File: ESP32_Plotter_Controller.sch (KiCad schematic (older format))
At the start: 45 parts, among them J1 ARM JTAG 10pin, J10 Pen Lift, J11 Vselect, J12 X Motor, J13 Y Motor, J14 Neo Pixel LEDs, J15 Pen Direction, J16 Aux Port (I2C), J17 USB_B_Micro, J18 E-Stop, J19 Y Limit Switch, J2 Power, J3 5V Aux, J4 Vin Aux, J5 X Limit Switch, J6 Aux Port (SPI), J7 X Limit, J8 Micro_SD_Card_TF-01A, J9 Y Limit, SW1 RESET, SW2 BOOT, U1 ESP32-WROOM-32D, U2 TMC2130, U3 TMC2130, U4 XL1509, U5 CH340C, U6 AMS1117-3.3

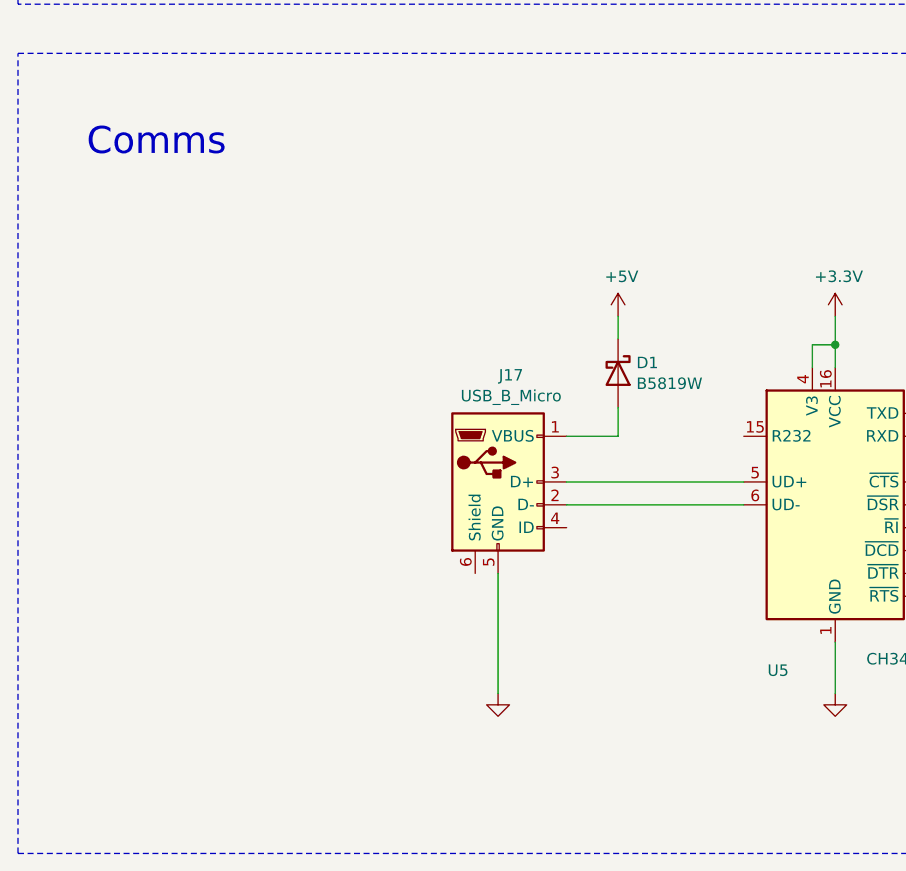
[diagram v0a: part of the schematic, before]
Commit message: Change to USB C connector
Had to move connectors around to make room.
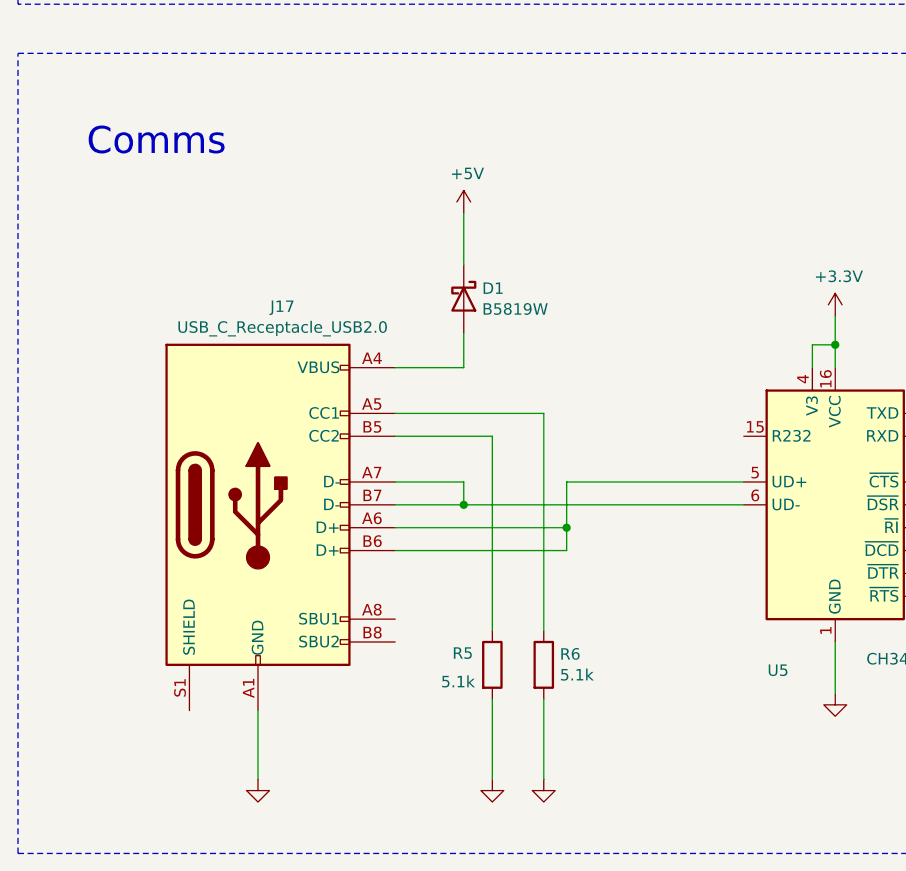
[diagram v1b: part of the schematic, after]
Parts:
- removed J17: USB_B_Micro, Connector_USB:USB_Micro-B_Molex-105017-0001, symbol Connector:USB_B_Micro
- added J17: USB_C_Receptacle_USB2.0, Connector_USB:USB_C_Receptacle_HRO_TYPE-C-31-M-12, symbol Connector:USB_C_Receptacle_USB2.0
- added R5, R6: 5.1k, Resistor_SMD:R_0603_1608Metric, symbol Device:R
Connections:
- net GND: now also J17.A1 (GND), J17.A12 (GND), J17.B1 (GND), J17.B12 (GND), R5.2, R6.2
- net at D1.2 (A): now also J17.A4 (VBUS), J17.A9 (VBUS), J17.B4 (VBUS), J17.B9 (VBUS)
- net at U5.5 (UD+): now also J17.A6 (D+), J17.B6 (D+)
- net at U5.6 (UD-): now also J17.A7 (D-), J17.B7 (D-)
- new net: J17.A5 (CC1), R6.1
- new net: J17.B5 (CC2), R5.1
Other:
- moved on the sheet: D1
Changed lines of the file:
@@
 	4325 12250 4325 12475
-$Comp
-L Connector:USB_B_Micro J17
-U 1 1 618FF665
-P 2850 11550
-F 0 "J17" H 2907 12017 50  0000 C CNN
-F 1 "USB_B_Micro" H 2907 11926 50  0000 C CNN
-F 2 "Connector_USB:USB_Micro-B_Molex-105017-0001" H 3000 11500 50  0001 C CNN
-F 3 "~" H 3000 11500 50  0001 C CNN
-F 4 "C381143" H 2850 11550 50  0001 C CNN "LCSC"
-	1    2850 11550
-	1    0    0    -1
-$EndComp
 $Comp
 L power:GND #NetPort07
 U 1 1 61900AC5
-P 2850 12475
-F 0 "#NetPort07" H 2850 12475 50  0001 C CNN
-F 1 "GND" H 2850 12475 50  0001 C CNN
-F 2 "" H 2850 12475 50  0001 C CNN
-F 3 "" H 2850 12475 50  0001 C CNN
-	1    2850 12475
-	1    0    0    -1
-$EndComp
-Wire Wire Line
-	2850 12475 2850 11950
-Wire Wire Line
-	3150 11650 3925 11650
+P 1800 12850
+F 0 "#NetPort07" H 1800 12850 50  0001 C CNN
+F 1 "GND" H 1800 12850 50  0001 C CNN
+F 2 "" H 1800 12850 50  0001 C CNN
+F 3 "" H 1800 12850 50  0001 C CNN
+	1    1800 12850
+	1    0    0    -1
+$EndComp
 Wire Wire Line
 	3150 11550 3925 11550
@@
 L Device:D_Schottky D1
 U 1 1 61647E81
-P 3375 11075
-F 0 "D1" V 3329 11155 50  0000 L CNN
-F 1 "B5819W" V 3420 11155 50  0000 L CNN
-F 2 "Diode_SMD:D_SOD-123" H 3375 11075 50  0001 C CNN
-F 3 "https://datasheet.lcsc.com/szlcsc/Changjiang-Electronics-Tech-CJ-B5819W_C8598.pdf" H 3375 11075 50  0001 C CNN
-	1    3375 11075
+P 2700 10750
+F 0 "D1" V 2654 10830 50  0000 L CNN
+F 1 "B5819W" V 2745 10830 50  0000 L CNN
+F 2 "Diode_SMD:D_SOD-123" H 2700 10750 50  0001 C CNN
+F 3 "https://datasheet.lcsc.com/szlcsc/Changjiang-Electronics-Tech-CJ-B5819W_C8598.pdf" H 2700 10750 50  0001 C CNN
+	1    2700 10750
 	0    1    1    0
 $EndComp
@@
 L power:+5V #PWR0105
 U 1 1 61649438
-P 3375 10825
-F 0 "#PWR0105" H 3375 10675 50  0001 C CNN
-F 1 "+5V" H 3390 10998 50  0000 C CNN
-F 2 "" H 3375 10825 50  0001 C CNN
-F 3 "" H 3375 10825 50  0001 C CNN
-	1    3375 10825
-	1    0    0    -1
-$EndComp
-Wire Wire Line
-	3150 11350 3375 11350
-Wire Wire Line
-	3375 11225 3375 11350
-Wire Wire Line
-	3375 10925 3375 10825
+P 2700 10375
+F 0 "#PWR0105" H 2700 10225 50  0001 C CNN
+F 1 "+5V" H 2715 10548 50  0000 C CNN
+F 2 "" H 2700 10375 50  0001 C CNN
+F 3 "" H 2700 10375 50  0001 C CNN
+	1    2700 10375
+	1    0    0    -1
+$EndComp
+$Comp
+L Connector:USB_C_Receptacle_USB2.0 J17
+U 1 1 617C3A54
+P 1800 11650
+F 0 "J17" H 1907 12517 50  0000 C CNN
+F 1 "USB_C_Receptacle_USB2.0" H 1907 12426 50  0000 C CNN
+F 2 "Connector_USB:USB_C_Receptacle_HRO_TYPE-C-31-M-12" H 1950 11650 50  0001 C CNN
+F 3 "https://www.usb.org/sites/default/files/documents/usb_type-c.zip" H 1950 11650 50  0001 C CNN
+F 4 "C165948 (TYPE-C-31-M-12)" H 1800 11650 50  0001 C CNN "LCSC"
+	1    1800 11650
+	1    0    0    -1
+$EndComp
+Wire Wire Line
+	2400 11650 2700 11650
+Wire Wire Line
+	2400 11550 2700 11550
+Wire Wire Line
+	2700 11550 2700 11650
+Connection ~ 2700 11650
+Wire Wire Line
+	2700 11650 3925 11650
+Wire Wire Line
+	2400 11750 3150 11750
+Wire Wire Line
+	3150 11750 3150 11550
+Wire Wire Line
+	2400 11850 3150 11850
+Wire Wire Line
+	3150 11850 3150 11750
+Connection ~ 3150 11750
+Wire Wire Line
+	2400 11050 2700 11050
+Wire Wire Line
+	2700 11050 2700 10900
+Wire Wire Line
+	2700 10600 2700 10375
+Wire Wire Line
+	1800 12850 1800 12550
+$Comp
+L Device:R R5
+U 1 1 6185A8A4
+P 2825 12350
+F 0 "R5" H 2650 12400 50  0000 L CNN
+F 1 "5.1k" H 2600 12275 50  0000 L CNN
+F 2 "Resistor_SMD:R_0603_1608Metric" V 2755 12350 50  0001 C CNN
+F 3 "~" H 2825 12350 50  0001 C CNN
+	1    2825 12350
+	1    0    0    -1
+$EndComp
+$Comp
+L Device:R R6
+U 1 1 6185BBB3
+P 3050 12350
+F 0 "R6" H 3120 12396 50  0000 L CNN
+F 1 "5.1k" H 3120 12305 50  0000 L CNN
+F 2 "Resistor_SMD:R_0603_1608Metric" V 2980 12350 50  0001 C CNN
+F 3 "~" H 3050 12350 50  0001 C CNN
+	1    3050 12350
+	1    0    0    -1
+$EndComp
+Wire Wire Line
+	2400 11250 3050 11250
+Wire Wire Line
+	3050 11250 3050 12200
+Wire Wire Line
+	2400 11350 2825 11350
+Wire Wire Line
+	2825 11350 2825 12200
+$Comp
+L power:GND #NetPort015
+U 1 1 61888507
+P 2825 12850
+F 0 "#NetPort015" H 2825 12850 50  0001 C CNN
+F 1 "GND" H 2825 12850 50  0001 C CNN
+F 2 "" H 2825 12850 50  0001 C CNN
+F 3 "" H 2825 12850 50  0001 C CNN
+	1    2825 12850
+	1    0    0    -1
+$EndComp
+$Comp
+L power:GND #NetPort016
+U 1 1 618889F6
+P 3050 12850
+F 0 "#NetPort016" H 3050 12850 50  0001 C CNN
+F 1 "GND" H 3050 12850 50  0001 C CNN
+F 2 "" H 3050 12850 50  0001 C CNN
+F 3 "" H 3050 12850 50  0001 C CNN
+	1    3050 12850
+	1    0    0    -1
+$EndComp
+Wire Wire Line
+	2825 12850 2825 12500
+Wire Wire Line
+	3050 12850 3050 12500
 $EndSCHEMATC

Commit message: RevB1 commit before cleanup
I wanted to be sure I didn't delete something I needed later, so this commit is all files in whatever state. In the next commit I will remove everything I think I no longer need so the repo is a bit cleaner and easier to see what files are important.
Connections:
- net GND: now also U1.39 (GND)
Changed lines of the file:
@@
 Wire Wire Line
 	3050 12850 3050 12500
+Wire Wire Line
+	4925 1775 4925 1750
+Wire Wire Line
+	4925 1750 3525 1750
+Wire Wire Line
+	3525 1750 3525 1975
+Connection ~ 3525 1975
 $EndSCHEMATC

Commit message: Add pull-up resistors to EN and IO0
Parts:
- added R7, R8: 10k, symbol Device:R
- J17: symbol Connector:USB_C_Receptacle_USB2.0 -> ESP32_Plotter_Controller-rescue:USB_C_Receptacle_USB2.0-Connector
- U5: symbol Interface_USB:CH340C -> ESP32_Plotter_Controller-rescue:CH340C-Interface_USB
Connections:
- wire segments 269 -> 278
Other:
- moved on the sheet: J18
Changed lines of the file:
@@
 L power:+3.3V #PWR02
 U 1 1 6168FE53
-P 3400 1800
-F 0 "#PWR02" H 3400 1650 50  0001 C CNN
-F 1 "+3.3V" H 3415 1973 50  0000 C CNN
-F 2 "" H 3400 1800 50  0001 C CNN
-F 3 "" H 3400 1800 50  0001 C CNN
-	1    3400 1800
-	1    0    0    -1
-$EndComp
-Wire Wire Line
-	3400 2075 3400 1800
+P 3400 1535
+F 0 "#PWR02" H 3400 1385 50  0001 C CNN
+F 1 "+3.3V" H 3415 1708 50  0000 C CNN
+F 2 "" H 3400 1535 50  0001 C CNN
+F 3 "" H 3400 1535 50  0001 C CNN
+	1    3400 1535
+	1    0    0    -1
+$EndComp
 $Comp
 L power:GND #NetPort09
@@
 	750  9675 8450 9675
 $Comp
-L Interface_USB:CH340C U5
+L ESP32_Plotter_Controller-rescue:CH340C-Interface_USB U5
 U 1 1 618C1A96
 P 4325 11650
@@
 	7600 4250 8125 4250
 Wire Wire Line
-	3775 2175 2775 2175
-Wire Wire Line
-	5475 3275 6325 3275
+	3775 2175 3090 2175
+Wire Wire Line
+	5475 3275 5585 3275
 Text Label 6325 3275 2    50   ~ 0
 IO0
@@
 L Connector:Conn_01x02_Male J18
 U 1 1 61ACBD71
-P 7020 3510
-F 0 "J18" H 7128 3691 50  0000 C CNN
-F 1 "E-Stop" H 7128 3600 50  0000 C CNN
-F 2 "Connector_JST:JST_PH_S2B-PH-K_1x02_P2.00mm_Horizontal" H 7020 3510 50  0001 C CNN
-F 3 "~" H 7020 3510 50  0001 C CNN
-F 4 "C16965 (JST PH TH RA), C47647 (JST PH SMT RA)" H 7020 3510 50  0001 C CNN "LCSC"
-	1    7020 3510
-	1    0    0    -1
-$EndComp
-Wire Wire Line
-	7220 3610 7520 3610
-Wire Wire Line
-	7220 3510 8270 3510
-Wire Wire Line
-	7520 3745 7520 3610
-Text Label 8270 3510 2    50   ~ 0
+P 6920 2835
+F 0 "J18" H 7028 3016 50  0000 C CNN
+F 1 "E-Stop" H 7028 2925 50  0000 C CNN
+F 2 "Connector_JST:JST_PH_S2B-PH-K_1x02_P2.00mm_Horizontal" H 6920 2835 50  0001 C CNN
+F 3 "~" H 6920 2835 50  0001 C CNN
+F 4 "C16965 (JST PH TH RA), C47647 (JST PH SMT RA)" H 6920 2835 50  0001 C CNN "LCSC"
+	1    6920 2835
+	1    0    0    -1
+$EndComp
+Wire Wire Line
+	7120 2935 7420 2935
+Wire Wire Line
+	7120 2835 8170 2835
+Wire Wire Line
+	7420 3070 7420 2935
+Text Label 8170 2835 2    50   ~ 0
 IO0
 $Comp
 L power:GND #NetPort014
 U 1 1 61ACC537
-P 7520 3745
-F 0 "#NetPort014" H 7520 3745 50  0001 C CNN
-F 1 "GND" H 7520 3745 50  0001 C CNN
-F 2 "" H 7520 3745 50  0001 C CNN
-F 3 "" H 7520 3745 50  0001 C CNN
-	1    7520 3745
+P 7420 3070
+F 0 "#NetPort014" H 7420 3070 50  0001 C CNN
+F 1 "GND" H 7420 3070 50  0001 C CNN
+F 2 "" H 7420 3070 50  0001 C CNN
+F 3 "" H 7420 3070 50  0001 C CNN
+	1    7420 3070
 	1    0    0    -1
 $EndComp
@@
 $EndComp
 $Comp
-L Connector:USB_C_Receptacle_USB2.0 J17
+L ESP32_Plotter_Controller-rescue:USB_C_Receptacle_USB2.0-Connector J17
 U 1 1 617C3A54
 P 1800 11650
@@
 	3525 1750 3525 1975
 Connection ~ 3525 1975
+$Comp
+L Device:R R7
+U 1 1 61DBB1E2
+P 3090 1940
+F 0 "R7" H 3160 1986 50  0000 L CNN
+F 1 "10k" H 3160 1895 50  0000 L CNN
+F 2 "" V 3020 1940 50  0001 C CNN
+F 3 "~" H 3090 1940 50  0001 C CNN
+	1    3090 1940
+	1    0    0    -1
+$EndComp
+$Comp
+L Device:R R8
+U 1 1 61E11249
+P 5585 1705
+F 0 "R8" H 5425 1765 50  0000 L CNN
+F 1 "10k" H 5390 1665 50  0000 L CNN
+F 2 "" V 5515 1705 50  0001 C CNN
+F 3 "~" H 5585 1705 50  0001 C CNN
+	1    5585 1705
+	1    0    0    -1
+$EndComp
+Wire Wire Line
+	5585 1465 5905 1465
+Wire Wire Line
+	5585 1555 5585 1465
+Wire Wire Line
+	5585 1855 5585 3275
+Connection ~ 5585 3275
+Wire Wire Line
+	5585 3275 6325 3275
+Wire Wire Line
+	3090 2090 3090 2175
+Connection ~ 3090 2175
+Wire Wire Line
+	3090 2175 2775 2175
+Wire Wire Line
+	3090 1740 3090 1790
+Wire Wire Line
+	3400 1535 3400 1740
+Wire Wire Line
+	3090 1740 3400 1740
+Connection ~ 3400 1740
+Wire Wire Line
+	3400 1740 3400 2075
 $EndSCHEMATC

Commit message: Add LCSC part no for SD socket
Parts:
- J8: LCSC (none) -> C91145
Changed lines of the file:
@@
 F 2 "custom:HK-TF01A" H 12700 8510 50  0001 C CNN
 F 3 "http://katalog.we-online.de/em/datasheet/693072010801.pdf" H 11550 8210 50  0001 C CNN
+F 4 "C91145 " H 11550 8210 50  0001 C CNN "LCSC"
 	1    11550 8210
 	1    0    0    -1

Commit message: Fix SD card footprint and add pull-up resistors
Rev B was using an old and incorrect footprint causing a 3.3v short to ground when an SD card was inserted. Update to use the fixed footprint.

Added pull-up resistors for EN and IO0 (Boot mode). On test board, IO0 appeared to be pulled permanently low. It could be programmed but would not boot. It may only be necessary for EN to be pulled high but added the pull-up for IO0 just incase.
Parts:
- J17: symbol ESP32_Plotter_Controller-rescue:USB_C_Receptacle_USB2.0-Connector -> Connector:USB_C_Receptacle_USB2.0
- R7, R8: footprint (none) -> Resistor_SMD:R_0603_1608Metric
- U5: symbol ESP32_Plotter_Controller-rescue:CH340C-Interface_USB -> Interface_USB:CH340C
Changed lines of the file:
@@
 	750  9675 8450 9675
 $Comp
-L ESP32_Plotter_Controller-rescue:CH340C-Interface_USB U5
+L Interface_USB:CH340C U5
 U 1 1 618C1A96
 P 4325 11650
@@
 $EndComp
 $Comp
-L ESP32_Plotter_Controller-rescue:USB_C_Receptacle_USB2.0-Connector J17
+L Connector:USB_C_Receptacle_USB2.0 J17
 U 1 1 617C3A54
 P 1800 11650
@@
 F 0 "R7" H 3160 1986 50  0000 L CNN
 F 1 "10k" H 3160 1895 50  0000 L CNN
-F 2 "" V 3020 1940 50  0001 C CNN
+F 2 "Resistor_SMD:R_0603_1608Metric" V 3020 1940 50  0001 C CNN
 F 3 "~" H 3090 1940 50  0001 C CNN
 	1    3090 1940
@@
 F 0 "R8" H 5425 1765 50  0000 L CNN
 F 1 "10k" H 5390 1665 50  0000 L CNN
-F 2 "" V 5515 1705 50  0001 C CNN
+F 2 "Resistor_SMD:R_0603_1608Metric" V 5515 1705 50  0001 C CNN
 F 3 "~" H 5585 1705 50  0001 C CNN
 	1    5585 1705

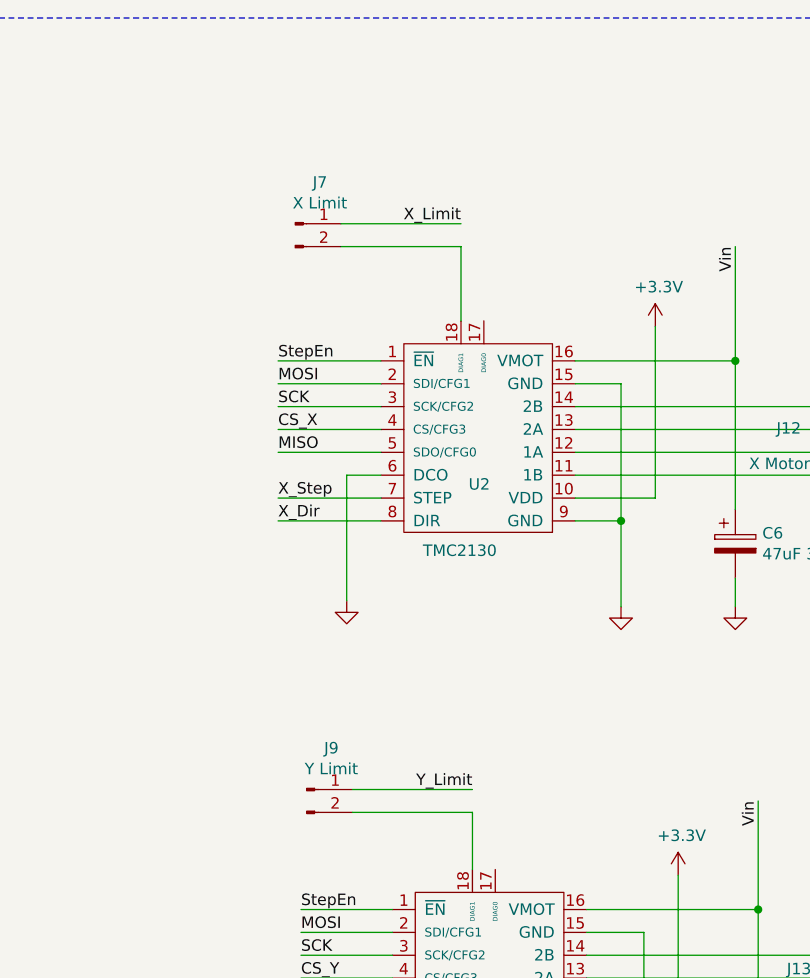
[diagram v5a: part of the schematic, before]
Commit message: Add pull-ups and manually tweak some routes
Added pull-ups for EN, Bpot, X_Limit & Y_Limit.
Re-routed some tracks to improve thermal ground on ESP32 module and to allow for better Gnd fills.
Regenerated Gerber files to include footprint values on front silkscreen.
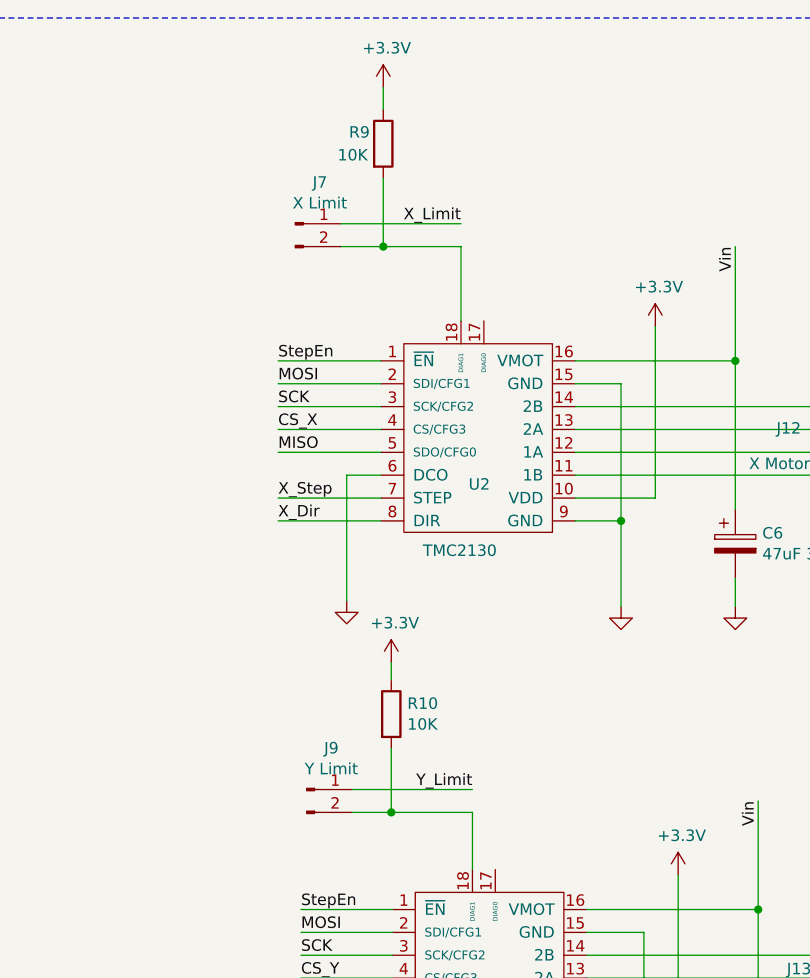
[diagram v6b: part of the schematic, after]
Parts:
- added R10, R9: 10K, Resistor_SMD:R_0603_1608Metric, symbol Device:R
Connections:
- net +3V3: now also R10.1, R9.1
- net at J7.2 (Pin_2), U2.18 (DIAG1): now also R9.2
- net at J9.2 (Pin_2), U3.18 (DIAG1): now also R10.2
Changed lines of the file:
@@
 $EndComp
 Wire Wire Line
-	15675 1635 16200 1635
-Wire Wire Line
-	15675 1735 16200 1735
-Wire Wire Line
-	15725 4110 16250 4110
-Wire Wire Line
-	15725 4210 16250 4210
+	15675 1735 15860 1735
+Wire Wire Line
+	15725 4210 15895 4210
 $Comp
 L Connector:Conn_01x03_Male J10
@@
 Wire Wire Line
 	3400 1740 3400 2075
+$Comp
+L Device:R R10
+U 1 1 61DFE2BA
+P 15895 3780
+F 0 "R10" H 15965 3826 50  0000 L CNN
+F 1 "10K" H 15965 3735 50  0000 L CNN
+F 2 "Resistor_SMD:R_0603_1608Metric" V 15825 3780 50  0001 C CNN
+F 3 "~" H 15895 3780 50  0001 C CNN
+	1    15895 3780
+	1    0    0    -1
+$EndComp
+$Comp
+L Device:R R9
+U 1 1 61DFE2C0
+P 15860 1285
+F 0 "R9" H 15710 1335 50  0000 L CNN
+F 1 "10K" H 15660 1235 50  0000 L CNN
+F 2 "Resistor_SMD:R_0603_1608Metric" V 15790 1285 50  0001 C CNN
+F 3 "~" H 15860 1285 50  0001 C CNN
+	1    15860 1285
+	1    0    0    -1
+$EndComp
+$Comp
+L power:+3.3V #PWR018
+U 1 1 61DFE2C6
+P 15860 1040
+F 0 "#PWR018" H 15860 890 50  0001 C CNN
+F 1 "+3.3V" H 15875 1213 50  0000 C CNN
+F 2 "" H 15860 1040 50  0001 C CNN
+F 3 "" H 15860 1040 50  0001 C CNN
+	1    15860 1040
+	1    0    0    -1
+$EndComp
+Wire Wire Line
+	15860 1135 15860 1040
+$Comp
+L power:+3.3V #PWR019
+U 1 1 61E624E4
+P 15895 3555
+F 0 "#PWR019" H 15895 3405 50  0001 C CNN
+F 1 "+3.3V" H 15910 3728 50  0000 C CNN
+F 2 "" H 15895 3555 50  0001 C CNN
+F 3 "" H 15895 3555 50  0001 C CNN
+	1    15895 3555
+	1    0    0    -1
+$EndComp
+Wire Wire Line
+	15895 3555 15895 3630
+Wire Wire Line
+	15675 1635 16200 1635
+Wire Wire Line
+	15860 1435 15860 1735
+Connection ~ 15860 1735
+Wire Wire Line
+	15860 1735 16200 1735
+Wire Wire Line
+	15725 4110 16250 4110
+Wire Wire Line
+	15895 3930 15895 4210
+Connection ~ 15895 4210
+Wire Wire Line
+	15895 4210 16250 4210
 $EndSCHEMATC

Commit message: Update component values
Some 10k resistors were using the value 10k vs 10K so weren't grouped correctly.
Some 100nF capacitors were shown as 0.1uF so weren't grouped correctly.
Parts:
- C11, C8: value 0.1uF -> 100nF
- R10, R3, R4, R9: value 10K -> 10k
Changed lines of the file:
@@
 P 6055 1705
 F 0 "R4" H 6125 1751 50  0000 L CNN
-F 1 "10K" H 6125 1660 50  0000 L CNN
+F 1 "10k" H 6125 1660 50  0000 L CNN
 F 2 "Resistor_SMD:R_0603_1608Metric" V 5985 1705 50  0001 C CNN
 F 3 "~" H 6055 1705 50  0001 C CNN
@@
 P 5905 1705
 F 0 "R3" H 5755 1755 50  0000 L CNN
-F 1 "10K" H 5705 1655 50  0000 L CNN
+F 1 "10k" H 5705 1655 50  0000 L CNN
 F 2 "Resistor_SMD:R_0603_1608Metric" V 5835 1705 50  0001 C CNN
 F 3 "~" H 5905 1705 50  0001 C CNN
@@
 P 7300 4500
 F 0 "C11" V 7450 4500 50  0000 C CNN
-F 1 "0.1uF" V 7150 4500 50  0000 C CNN
+F 1 "100nF" V 7150 4500 50  0000 C CNN
 F 2 "Capacitor_SMD:C_0603_1608Metric" H 7338 4350 50  0001 C CNN
 F 3 "~" H 7300 4500 50  0001 C CNN
@@
 P 1975 4500
 F 0 "C8" V 1800 4500 50  0000 C CNN
-F 1 "0.1uF" V 2125 4500 50  0000 C CNN
+F 1 "100nF" V 2125 4500 50  0000 C CNN
 F 2 "Capacitor_SMD:C_0603_1608Metric" H 2013 4350 50  0001 C CNN
 F 3 "~" H 1975 4500 50  0001 C CNN
@@
 P 15895 3780
 F 0 "R10" H 15965 3826 50  0000 L CNN
-F 1 "10K" H 15965 3735 50  0000 L CNN
+F 1 "10k" H 15965 3735 50  0000 L CNN
 F 2 "Resistor_SMD:R_0603_1608Metric" V 15825 3780 50  0001 C CNN
 F 3 "~" H 15895 3780 50  0001 C CNN
@@
 P 15860 1285
 F 0 "R9" H 15710 1335 50  0000 L CNN
-F 1 "10K" H 15660 1235 50  0000 L CNN
+F 1 "10k" H 15660 1235 50  0000 L CNN
 F 2 "Resistor_SMD:R_0603_1608Metric" V 15790 1285 50  0001 C CNN
 F 3 "~" H 15860 1285 50  0001 C CNN
